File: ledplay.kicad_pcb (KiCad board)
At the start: 4 copper layers, 50 x 50 mm, 87 parts, among them J1 UART_CONN, J2 CORTEX_DEBUG, P1 PWRCON_01X02, P2 CONN_01X05, P3 CONN_01X05, P4 CONN_01X05, P5 CONN_01X05, P6 CONN_01X02, Q1 BSS138, Q2 BSS138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

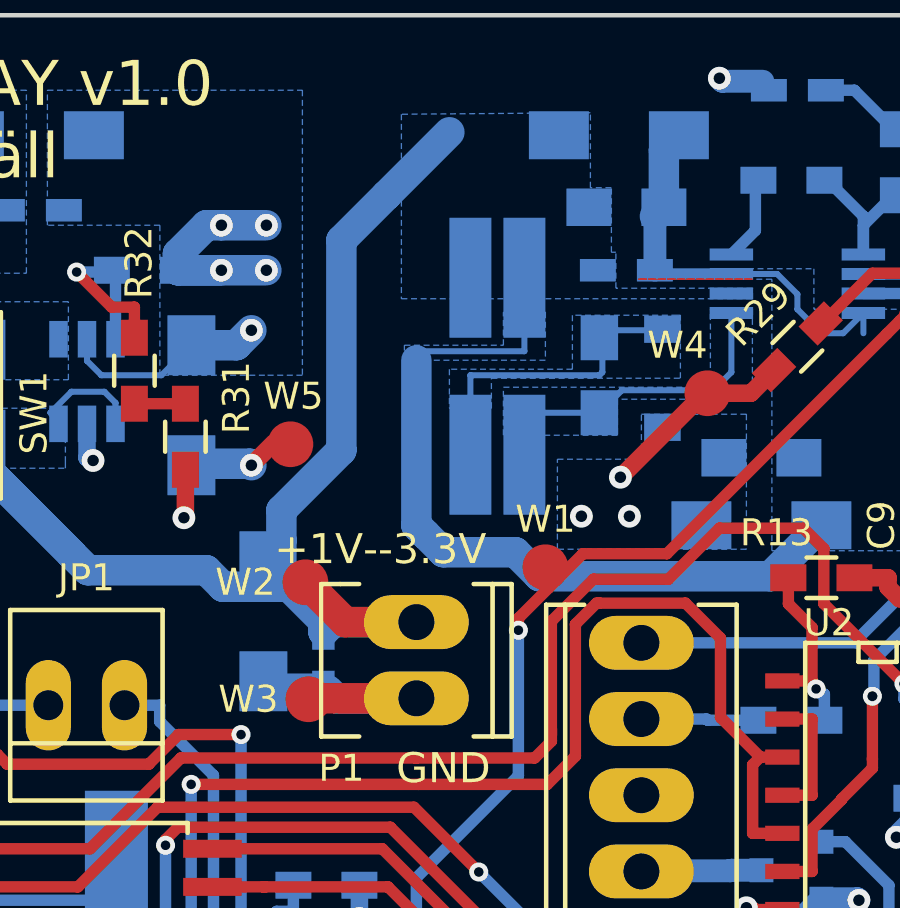
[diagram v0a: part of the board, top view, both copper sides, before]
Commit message: Fix layout and schema (as sent for production)
This matches hardware revision v1.0 sent for production.
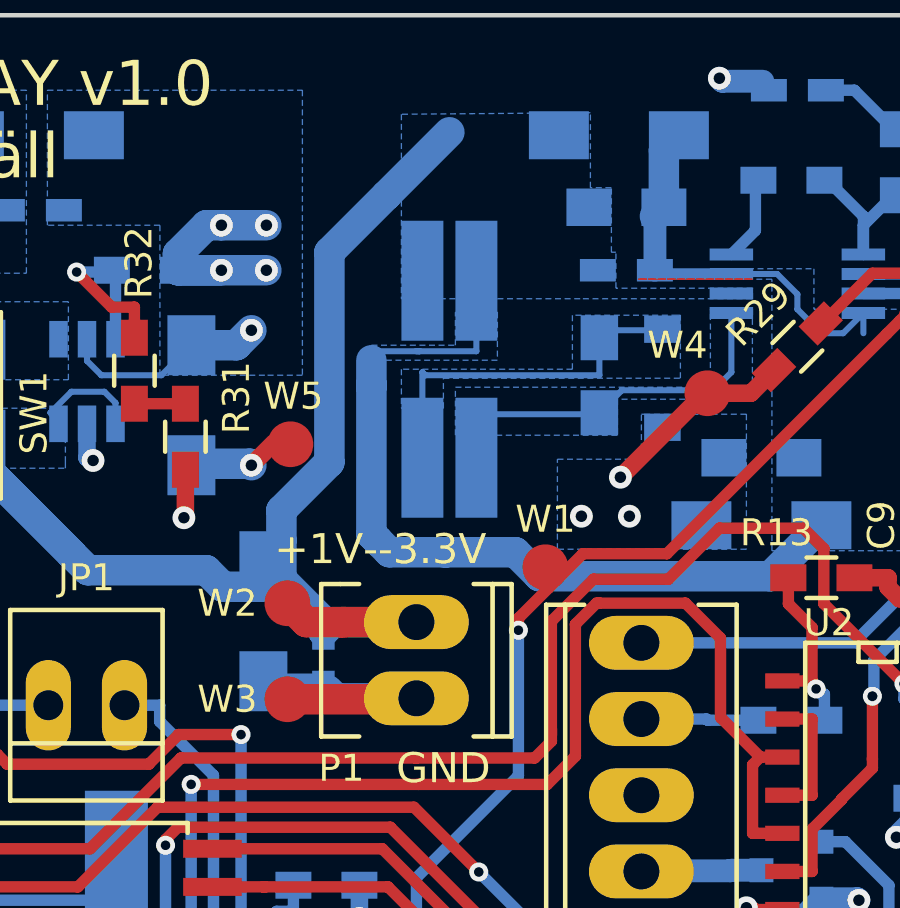
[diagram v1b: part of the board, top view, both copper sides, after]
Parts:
- moved L1 1.60 mm to (73.6, 61.8)
- moved W2 0.92 mm to (68.2, 69.6)
- moved W3 0.70 mm to (68.2, 72.8)
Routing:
- net GND: track 139.2 -> 142.8 mm
- net Net-(C21-Pad1): track 9.63 -> 12.7 mm
- net Net-(C21-Pad2): track 11.4 -> 13.2 mm
- net +BATT: track 51.5 -> 50.5 mm

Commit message: Fix power connector polarity
The power connector had the wrong polarity in the schematic. Fix it to
avoid confusion.
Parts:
- turned P1 to 90 degrees
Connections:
- P1 pad 1: +BATT -> GND
- P1 pad 2: GND -> +BATT
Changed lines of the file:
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@@
     (links 185)
     (no_connects 0)
-    (area 48.339258 49.0964 100.075001 101.636933)
+    (area 49.924999 49.924999 100.075001 100.075001)
     (thickness 1.6)
     (drawings 20)
@@
   )
   (setup
-    (last_trace_width 1.016)
+    (last_trace_width 0.381)
     (user_trace_width 0.2032)
     (user_trace_width 0.381)
@@
   )
   (module Sockets_MOLEX_KK-System:Socket_MOLEX-KK-RM2-54mm_Lock_2pin_straight (layer F.Cu)
-    (at 72.5 71.5 270)
+    (at 72.5 71.5 90)
     (descr "Socket, MOLEX, KK, RM 2.54mm, Lock, 2pin, straight,")
     (tags "Socket, MOLEX, KK, RM 2.54mm, Lock, 2pin, straight,")
-    (fp_text reference P1 (at 3.6 2.5 360) (layer F.SilkS)
-      (effects (font (size 0.9 0.9) (thickness 0.15)))
-    )
-    (fp_text value PWRCON_01X02 (at -0.635 5.08 270) (layer F.Fab)
+    (fp_text reference P1 (at 3.6 2.5 180) (layer F.SilkS)
+      (effects (font (size 0.9 0.9) (thickness 0.15)))
+    )
+    (fp_text value PWRCON_01X02 (at -0.635 5.08 90) (layer F.Fab)
       (effects (font (size 0.9 0.9) (thickness 0.15)))
     )
@@
     (fp_line (start 2.54 3.175) (end -2.54 3.175) (layer F.SilkS) (width 0.15))
     (fp_line (start -2.54 3.175) (end -2.54 2.54) (layer F.SilkS) (width 0.15))
-    (pad 1 thru_hole oval (at -1.27 0 270) (size 1.80086 3.50012) (drill 1.19888) (layers *.Cu *.Mask F.SilkS)
+    (pad 1 thru_hole oval (at -1.27 0 90) (size 1.80086 3.50012) (drill 1.19888) (layers *.Cu *.Mask F.SilkS)
+      (net 2 GND))
+    (pad 2 thru_hole oval (at 1.27 0 90) (size 1.80086 3.50012) (drill 1.19888) (layers *.Cu *.Mask F.SilkS)
       (net 1 +BATT))
-    (pad 2 thru_hole oval (at 1.27 0 270) (size 1.80086 3.50012) (drill 1.19888) (layers *.Cu *.Mask F.SilkS)
-      (net 2 GND))
   )
   (module Sockets_MOLEX_KK-System:Socket_MOLEX-KK-RM2-54mm_Lock_5pin_straight (layer F.Cu)
@@
   (gr_line (start 50 50) (end 100 50) (angle 90) (layer Edge.Cuts) (width 0.15))
   (segment (start 80.6 52.25) (end 80.6 52.2) (width 0.381) (layer GND.Cu) (net 0))
-  (segment (start 70 70.23) (end 68.83 70.23) (width 1.016) (layer F.Cu) (net 1))
-  (segment (start 68.83 70.23) (end 68.2 69.6) (width 1.016) (layer F.Cu) (net 1) (status 800000))
-  (segment (start 72.5 70.23) (end 70 70.23) (width 1.016) (layer F.Cu) (net 1))
-  (segment (start 70 70.23) (end 70.13 70.23) (width 1.016) (layer F.Cu) (net 1))
+  (segment (start 68.83 70.23) (end 68.2 69.6) (width 1.016) (layer F.Cu) (net 1))
   (segment (start 69.4 70.55) (end 69.4 70.2) (width 1.016) (layer B.Cu) (net 1))
   (segment (start 69.4 70.2) (end 67.4 68.2) (width 1.016) (layer B.Cu) (net 1))
@@
   (segment (start 62.47 63.62) (end 62.47 62.92) (width 0.2032) (layer B.Cu) (net 1))
   (segment (start 68 69.05) (end 68 67.5) (width 1.016) (layer B.Cu) (net 1))
-  (segment (start 68.2 72.8) (end 72.6 72.8) (width 1.016) (layer F.Cu) (net 2) (status C00000))
-  (segment (start 72.6 72.8) (end 72.5 72.77) (width 1.016) (layer F.Cu) (net 2) (status C00000))
+  (segment (start 70 70.23) (end 68.83 70.23) (width 1.016) (layer F.Cu) (net 1))
+  (segment (start 72.5 70.23) (end 70 70.23) (width 1.016) (layer F.Cu) (net 1))
+  (segment (start 70 70.23) (end 70.13 70.23) (width 1.016) (layer F.Cu) (net 1))
+  (segment (start 72.6 72.8) (end 72.5 72.77) (width 1.016) (layer F.Cu) (net 2))
+  (segment (start 72.5 72.77) (end 69.82 72.77) (width 1.016) (layer B.Cu) (net 2))
+  (segment (start 68.2 72.8) (end 72.6 72.8) (width 1.016) (layer F.Cu) (net 2))
   (segment (start 71 62.3) (end 71 61.5) (width 1.016) (layer B.Cu) (net 2))
   (segment (start 71.2 67.5) (end 71 67.3) (width 1.016) (layer B.Cu) (net 2))
@@
   (segment (start 69.5 72.5) (end 69.55 72.5) (width 0.762) (layer B.Cu) (net 2))
   (segment (start 69.55 72.5) (end 69.82 72.77) (width 1.016) (layer B.Cu) (net 2))
-  (segment (start 72.5 72.77) (end 69.82 72.77) (width 1.016) (layer B.Cu) (net 2))
   (segment (start 86.00076 79.45) (end 87.2 79.45) (width 0.762) (layer B.Cu) (net 2))
   (via (at 87.25 79.5) (size 0.762) (drill 0.381) (layers F.Cu B.Cu) (net 2))
